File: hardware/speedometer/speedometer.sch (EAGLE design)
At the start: 124 parts, among them IC1 PIC32MX274F256DT-I_PT, IC10 24LC024SN, IC11 MAX16054AZT+T, IC12 TPS63001DRCT, IC13 TPS63002DRCT, IC2 CSTCE8M00G55-R0, IC3 BQ27441DRZR-G1A, IC7 BQ24075RGTT, IC8 NRF24L01P-T, IC9 CSTCE16M0V53-R0, J1 10104111-0001LF, J2 BAT, J3 CONUFL001-SMD-T, J4 Right_sens, J5 Right, J6 Left_sens, J7 Left, Q1 BC817, Q2 BC817, Q3 BC817, Q4 BC817, U1 SN74AHC1G08DBVR

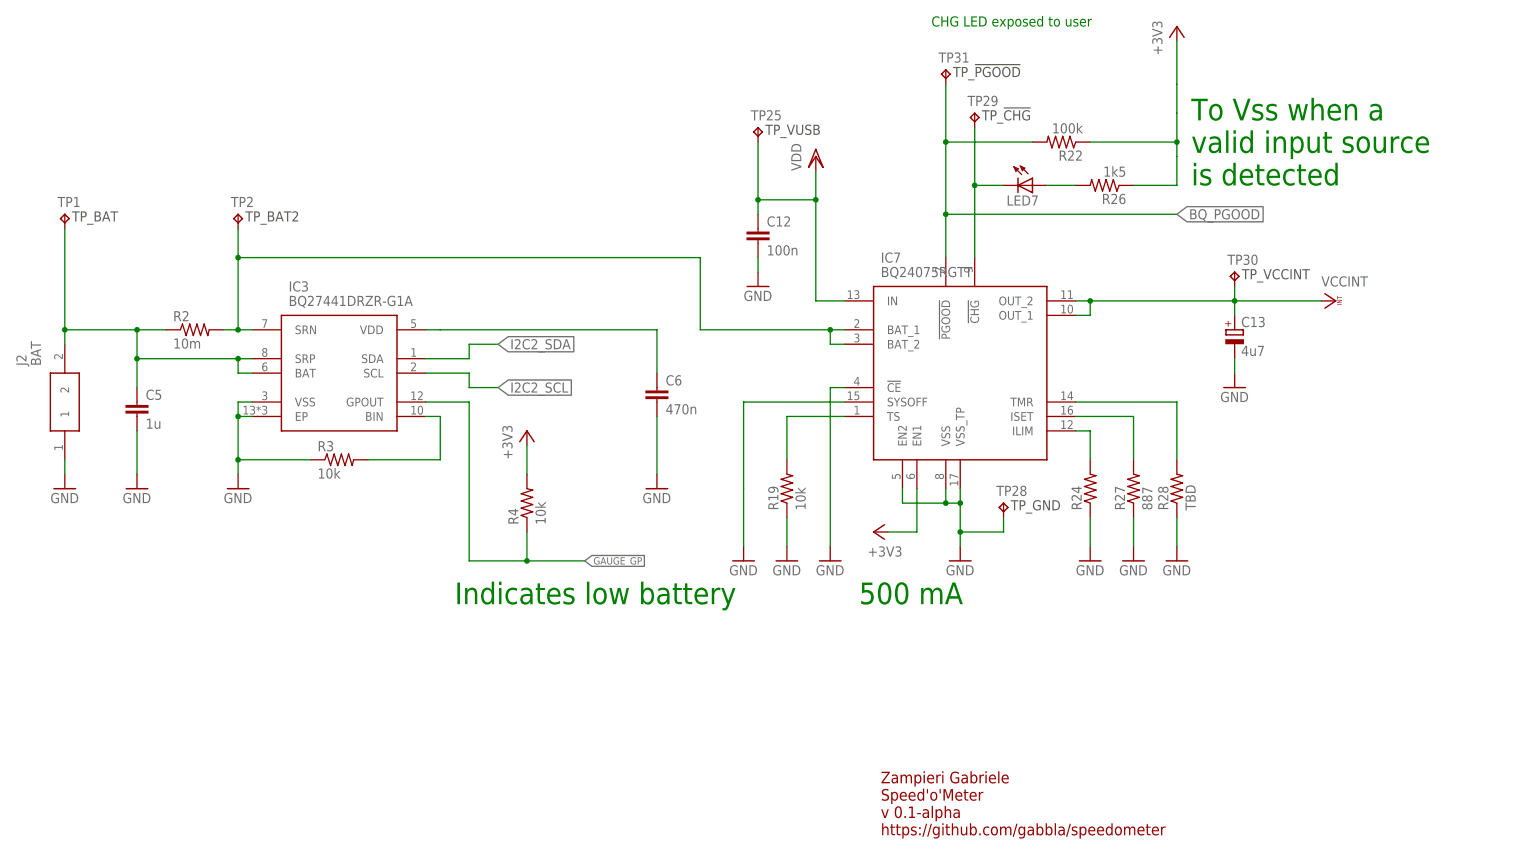
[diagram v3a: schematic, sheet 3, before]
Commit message: fixed led off while charging the board in off state
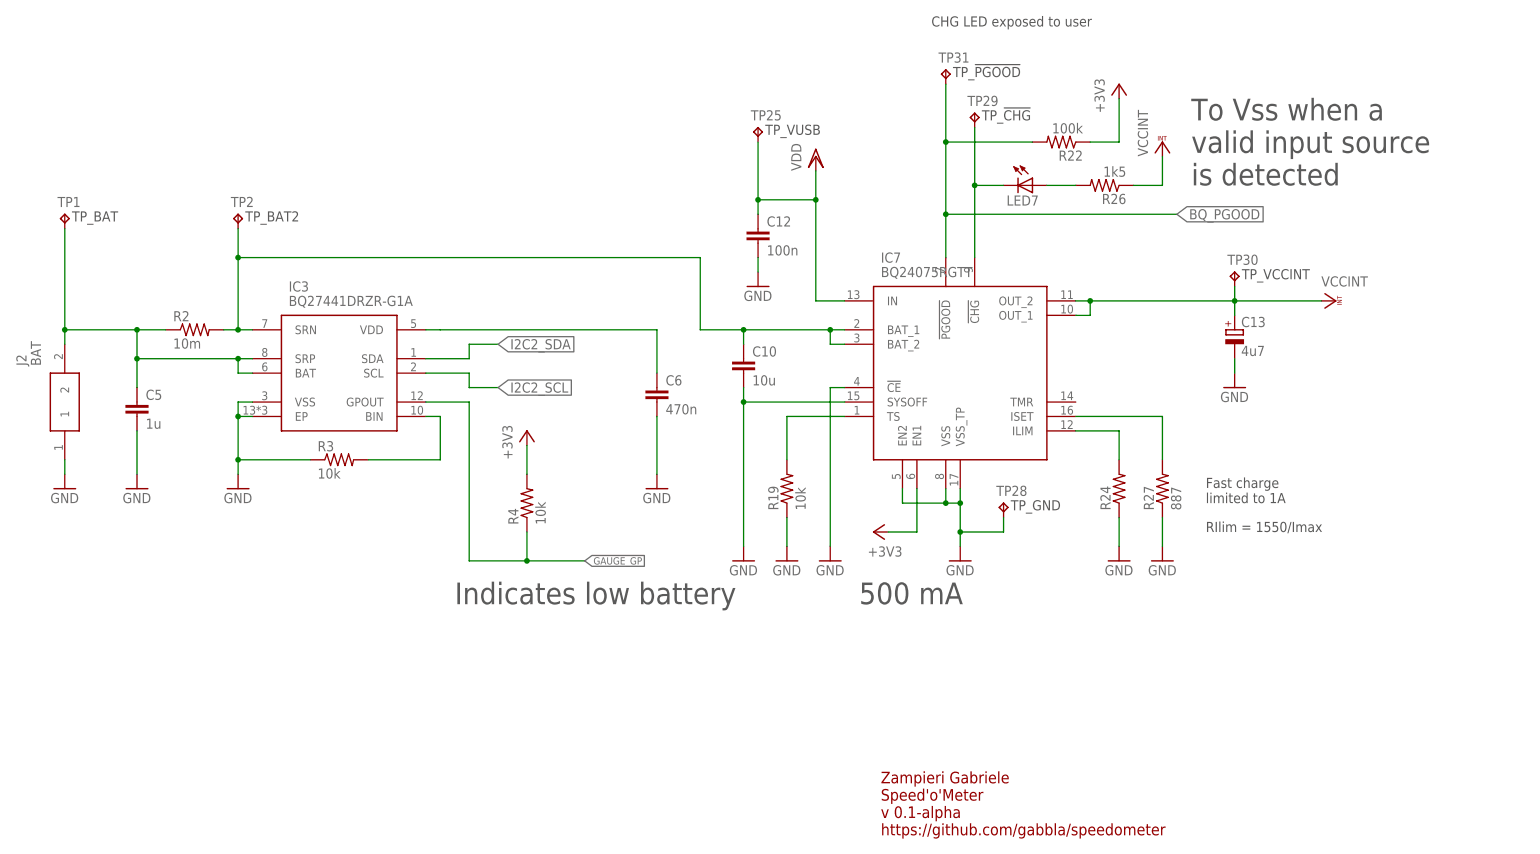
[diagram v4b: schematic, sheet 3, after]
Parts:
- removed R28: TBD, rcl:R-US_R0805
- added C10: 10u, rcl:C-EUC0603K
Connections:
- removed net N$14: IC7.TMR, R28.2
- net +3V3: no longer R26.1
- net GND: now also C10.2; no longer R28.1
- net N$43: now also C10.1
- net VCCINT: now also R26.1
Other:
- note added: "Fast charge limited to 1A"
- note added: "RIlim = 1550/Imax"
- moved on the sheet: R24, R27

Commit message: part renumbered
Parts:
- removed C29, C30: 10u, rcl:C-EUC0805K
- removed IC12: TPS63001DRCT, TPS63000DRCT:TPS63000DRCT
- removed IC13: TPS63002DRCT, TPS63000DRCT:TPS63000DRCT
- removed R35, R39: 100k, rcl:R-US_R0805
- removed R36, R37: 100, rcl:R-US_R0805
- removed R38: 10k, rcl:R-US_R0805
- removed TP25, TP31: TPB1,27, testpad:TPB1,27
- removed U$1: HM-11, HM11:HM-11
- added C11: 100n, rcl:C-EUC0603K
- added C16: 2n2, rcl:C-EUC0402K
- added IC4: BQ27441DRZR-G1A, BQ27441DRZR-G1A:BQ27441DRZR-G1A
- added IC5: BQ24075RGTT, BQ24075RGTT:BQ24075RGTT
- added IC6: NRF24L01P-T, nRF24L01P-T:NRF24L01P-T
- added R15, R33: 100k, rcl:R-US_R0805
- added R16: 1k5, rcl:R-US_R0805
- added R17: (no value), rcl:R-US_R0805
- added R31: 10k, rcl:R-US_R0805
- added TP14, TP9: TPB1,27, testpad:TPB1,27
- C1: value 10u -> 100n; device rcl:C-EUC0805K -> rcl:C-EUC0603
- C12: value 100n -> 4u7; device rcl:C-EUC0603K -> rcl:CPOL-EUSMCA
- C13: value 4u7 -> 10n; device rcl:CPOL-EUSMCA -> rcl:C-EUC0805K
- C14: value 10n -> 1n
- C15: value 1n -> 33n; device rcl:C-EUC0805K -> rcl:C-EUC0402K
- C17: value 33n -> 4p7
- C18: value 2n2 -> 1p5
- C19: value 4p7 -> 1p
- C20: value 1p5 -> 100n; device rcl:C-EUC0402K -> rcl:C-EUC0603K
- C21: value 1p -> 10u; device rcl:C-EUC0402K -> rcl:C-EUC0805K
- C22: value 100n -> 10u; device rcl:C-EUC0603K -> rcl:C-EUC0805K
- C3: value 100n -> 10u; device rcl:C-EUC0603 -> rcl:C-EUC0805K
- C5: value 1u -> 100n; device rcl:C-EUC0603K -> rcl:C-EUC0603
- C6: value 470n -> 100n; device rcl:C-EUC0603K -> rcl:C-EUC0603
- C8: value 100n -> 1u; device rcl:C-EUC0603 -> rcl:C-EUC0603K
- C9: value 100n -> 470n; device rcl:C-EUC0603 -> rcl:C-EUC0603K
- IC10: value 24LC024SN -> TPS63001DRCT; device microchip:24LC024SN -> TPS63000DRCT:TPS63000DRCT
- IC11: value MAX16054AZT+T -> TPS63002DRCT; device MAX16054AZT+T:MAX16054AZT+T -> TPS63000DRCT:TPS63000DRCT
- IC3: value BQ27441DRZR-G1A -> HM-11; device BQ27441DRZR-G1A:BQ27441DRZR-G1A -> HM11:HM-11
- IC7: value BQ24075RGTT -> CSTCE16M0V53-R0; device BQ24075RGTT:BQ24075RGTT -> CSTCE12M0G15L99-R0:CSTCE12M0G15L99-R0
- IC8: value NRF24L01P-T -> 24LC024SN; device nRF24L01P-T:NRF24L01P-T -> microchip:24LC024SN
- IC9: value CSTCE16M0V53-R0 -> MAX16054AZT+T; device CSTCE12M0G15L99-R0:CSTCE12M0G15L99-R0 -> MAX16054AZT+T:MAX16054AZT+T
- JP2: device pinhead:PINHD-1X3 -> pinhead:PINHD-1X2
- JP3: device pinhead:PINHD-1X2 -> pinhead:PINHD-1X3
- LED1: device led:LED3MM -> led:LEDCHIPLED_0805
- LED2: device led:LEDCHIPLED_0805 -> led:LED3MM
- Q2: SPICEPREFIX Q -> (none)
- Q3: SPICEPREFIX (none) -> Q
- R11: value 470 -> 10m; device rcl:R-US_M0805 -> rcl:R-US_R2512; RS (none) -> 693-4381
- R13: value 1k -> 10k; device rcl:R-US_M0805 -> rcl:R-US_R0805
- R14: device rcl:R-US_M0805 -> rcl:R-US_R0805
- R18: value 100k -> 887; RS (none) -> 708-6111
- R19: value 10k -> 22k
- R2: value 10m -> 1k; device rcl:R-US_R2512 -> rcl:R-US_M0805; RS 693-4381 -> (none)
- R20, R25: value 10k -> 100k
- R21: value 10k -> 100; RS_PART_NUMBER (none) -> 740-8978
- R22: value 100k -> 100; RS_PART_NUMBER (none) -> 740-8978
- R23: value 100k -> 10k
- R24: value (none) -> 10k
- R26: value 1k5 -> 10k
- R27: value 887 -> 100k; RS 708-6111 -> (none)
- R3, R4: device rcl:R-US_R0805 -> rcl:R-US_M0805
- R34: value 22k -> 10k
- R7: value 10k -> 4k7
- R9: value 4k7 -> 470
- TP1: TP_SIGNAL_NAME TP_BAT -> TP_SCL
- TP10: TP_SIGNAL_NAME TP_SPI1_SCK -> BT_RX
- TP11: TP_SIGNAL_NAME TP_NRF_CE -> BT_RST
- TP12: TP_SIGNAL_NAME BT_TX -> BT_KEY
- TP13: TP_SIGNAL_NAME BT_RX -> TP_BAT
- TP15: TP_SIGNAL_NAME BT_RST -> TP_VUSB
- TP16: TP_SIGNAL_NAME BT_KEY -> TP_!PGOOD
- TP2: TP_SIGNAL_NAME TP_BAT2 -> TP_SDA
- TP3: TP_SIGNAL_NAME TP_SCL -> TP_SPI1_SDO
- TP4: TP_SIGNAL_NAME TP_SDA -> TP_SPI1_SDI
- TP5: TP_SIGNAL_NAME TP_SPI1_SDO -> TP_NRF_IRQ
- TP6: TP_SIGNAL_NAME TP_SPI1_SDI -> TP_NRF_CS
- TP7: TP_SIGNAL_NAME TP_NRF_IRQ -> TP_SPI1_SCK
- TP8: TP_SIGNAL_NAME TP_NRF_CS -> TP_NRF_CE
- renumbered ICSP to SV1, LED7 to LED3, LED8 to LED4, LED9 to LED5, R40 to R28, R41 to R29, R42 to R30, R43 to R32, TP28 to TP18, TP29 to TP17, TP30 to TP19, TP33 to TP20, TP34 to TP21, TP35 to TP22, TP36 to TP23, TP37 to TP24
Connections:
- net !BAT_CHG: now also IC5.!CHG; no longer IC7.!CHG
- net !MCLR: now also R2.1; no longer R13.1
- net +3V3: now also C1.1, C13.1, C20.1, C5.1, IC10.FB, IC10.VOUT, IC3.VCC, IC5.EN1, IC6.VDD_1, IC6.VDD_2, IC6.VDD_3, IC8.VCC, JP2.1, R13.2, R15.1, R26.2, R3.2, R34.2; no longer C15.1, C22.1, C3.1, C8.1, IC10.VCC, IC12.FB, IC12.VOUT, IC7.EN1, IC8.VDD_1, IC8.VDD_2, IC8.VDD_3, JP3.1, R22.1, R25.2, R35.2, R4.2, R9.2, U$1.VCC
- net +5V: now also IC11.FB, IC11.VOUT; no longer IC13.FB, IC13.VOUT
- net BL_TRIG: now also JP2.2, R4.2; no longer JP3.2, R14.2
- net BQ_PGOOD: now also IC5.!PGOOD, R15.2, TP16.TP; no longer IC7.!PGOOD, R22.2, TP31.TP
- net BT_RST: now also R7.1; no longer R9.1
- net GAUGE_GP: now also IC4.GPOUT, R13.1; no longer IC3.GPOUT, R4.1
- net GND: now also C11.2, C12.-, C13.2, C16.2, C20.2, IC10.PGND, IC11.PGND, IC3.GND, IC4.EP, IC4.VSS, IC5.!CE, IC5.EN2, IC5.SYSOFF, IC5.VSS, IC5.VSS_TP, IC6.TP_GND, IC6.VSS_1, IC6.VSS_2, IC6.VSS_3, IC6.VSS_4, IC7.2, IC8.A0, IC8.A1, IC8.A2, IC8.GND, IC8.WP, IC9.CLEAR, IC9.GND, JP3.3, LED2.C, R12.1, R17.1, R18.1, R19.2, R25.2, R27.2, R33.2, R4.1; no longer C12.2, C13.-, C18.2, C29.2, C30.2, IC10.A0, IC10.A1, IC10.A2, IC10.WP, IC11.CLEAR, IC12.GND, IC12.PGND, IC13.GND, IC13.PGND, IC3.EP, IC3.VSS, IC7.!CE, IC7.EN2, IC7.SYSOFF, IC7.VSS, IC7.VSS_TP, IC8.TP_GND, IC8.VSS_1, IC8.VSS_2, IC8.VSS_3, IC8.VSS_4, IC9.2, JP2.3, LED1.C, R18.2, R19.1, R23.2, R24.1, R27.1, R3.1, R34.2, R39.2, U$1.GND
- net I2C2_SCL: now also IC4.SCL, IC8.SCL, TP1.TP; no longer IC10.SCL, IC3.SCL, TP3.TP
- net I2C2_SDA: now also IC4.SDA, IC8.SDA, TP2.TP; no longer IC10.SDA, IC3.SDA, TP4.TP
- net INT_LEFT: now also R34.1; no longer R25.1
- net INT_RIGHT: now also Q1.C, R26.1; no longer Q3.C, R20.1
- net LED_HB: now also LED1.A; no longer LED2.A
- net N$1: now also IC3.!RESET, TP11.TP; no longer TP15.TP, U$1.!RESET
- net N$12: now also R16.2; no longer R26.2
- net N$13: now also R31.2, R33.1; no longer R21.2, R23.1
- net N$16: now also C9.1, IC4.VDD; no longer C6.1, IC3.VDD
- net N$17: now also Q3.C; no longer Q2.C
- net N$18: now also Q3.B; no longer Q2.B
- net N$2: now also IC3.PIO0/KEY, TP12.TP; no longer TP16.TP, U$1.PIO0/KEY
- net N$21: now also C3.1; no longer C1.1
- net N$22: now also IC6.XC2, IC7.1; no longer IC8.XC2, IC9.1
- net N$24: now also IC6.IREF, R19.1; no longer IC8.IREF, R34.1
- net N$25: now also C15.1, IC6.DVDD; no longer C17.1, IC8.DVDD
- net N$26: now also Q1.B, R23.2, R25.1; no longer Q3.B, R12.2, R18.1
- net N$27: now also R23.1; no longer R12.1
- net N$28: now also R31.1; no longer R21.1
- net N$29: now also LED1.C; no longer LED2.C
- net N$3: now also C8.1, IC4.BAT, IC4.SRP, R11.1, TP13.TP; no longer C5.1, IC3.BAT, IC3.SRP, R2.1, TP1.TP
- net N$30: now also IC4.BIN, R12.2; no longer IC3.BIN, R3.2
- net N$31: now also IC6.XC1, IC7.3; no longer IC8.XC1, IC9.3
- net N$32: now also IC6.ANT2; no longer IC8.ANT2
- net N$33: now also IC6.ANT1; no longer IC8.ANT1
- net N$34: now also IC10.L2; no longer IC12.L2
- net N$35: now also C16.1, C17.1, IC6.VDD_PA; no longer C18.1, C19.1, IC8.VDD_PA
- net N$36: now also C18.1; no longer C20.1
- net N$37: now also C18.2, C19.1; no longer C20.2, C21.1
- net N$38: now also Q2.C; no longer Q1.C
- net N$39: now also Q2.B, R24.2, R27.1; no longer Q1.B, R38.2, R39.1
- net N$4: now also IC3.PIO1/LED, R9.1; no longer R11.1, U$1.PIO1/LED
- net N$41: now also C6.1, R2.2, R3.1; no longer C9.1, R13.2, R7.1
- net N$42: now also R24.1; no longer R38.1
- net N$43: now also IC4.SRN, IC5.BAT_1, IC5.BAT_2, R11.2, TP14.TP; no longer IC3.SRN, IC7.BAT_1, IC7.BAT_2, R2.2, TP2.TP
- net N$5: now also IC10.L1; no longer IC12.L1
- net N$58: now also IC9.IN; no longer IC11.IN
- net N$59: now also IC11.L1; no longer IC13.L1
- net N$6: now also LED2.A, R9.2; no longer LED1.A, R11.2
- net N$60: now also IC10.PS/SYNC, IC10.VINA, R21.1; no longer IC12.PS/SYNC, IC12.VINA, R36.1
- net N$61: now also IC11.L2; no longer IC13.L2
- net N$62: now also IC11.PS/SYNC, IC11.VINA, R22.1; no longer IC13.PS/SYNC, IC13.VINA, R37.1
- net N$7: now also IC5.TS, R14.2; no longer IC7.TS, R19.2
- net N$8: now also IC5.ILIM, R17.2; no longer IC7.ILIM, R24.2
- net N$9: now also IC5.ISET, R18.2; no longer IC7.ISET, R27.2
- net NRF_!CS: now also IC6.CSN, TP6.TP; no longer IC8.CSN, TP8.TP
- net NRF_CE: now also IC6.CE, TP8.TP; no longer IC8.CE, TP11.TP
- net NRF_IRQ: now also IC6.IRQ, R20.1, TP5.TP; no longer IC8.IRQ, R35.1, TP7.TP
- net SPI1_SCK: now also IC6.SCK, TP7.TP; no longer IC8.SCK, TP10.TP
- net SPI1_SDI: now also IC6.MISO, TP4.TP; no longer IC8.MISO, TP6.TP
- net SPI1_SDO: now also IC6.MOSI, TP3.TP; no longer IC8.MOSI, TP5.TP
- net SYS_EN: now also IC10.EN, IC11.EN, IC9.OUT; no longer IC11.OUT, IC12.EN, IC13.EN
- net U1_RX: now also IC3.UART_TX, TP9.TP; no longer TP12.TP, U$1.UART_TX
- net U1_TX: now also IC3.UART_RX, TP10.TP; no longer TP13.TP, U$1.UART_RX
- net U2_RX: now also JP3.2; no longer JP2.2
- net U2_TX: now also JP3.1; no longer JP2.1
- net VCCINT: now also C12.+, C21.1, C22.1, IC10.VIN, IC11.VIN, IC5.OUT_1, IC5.OUT_2, IC9.VCC, R16.1, R21.2, R22.2; no longer C13.+, C29.1, C30.1, IC11.VCC, IC12.VIN, IC13.VIN, IC7.OUT_1, IC7.OUT_2, R26.1, R36.2, R37.2
- net VDD: now also C11.1, IC5.IN, TP15.TP; no longer C12.1, IC7.IN, TP25.TP

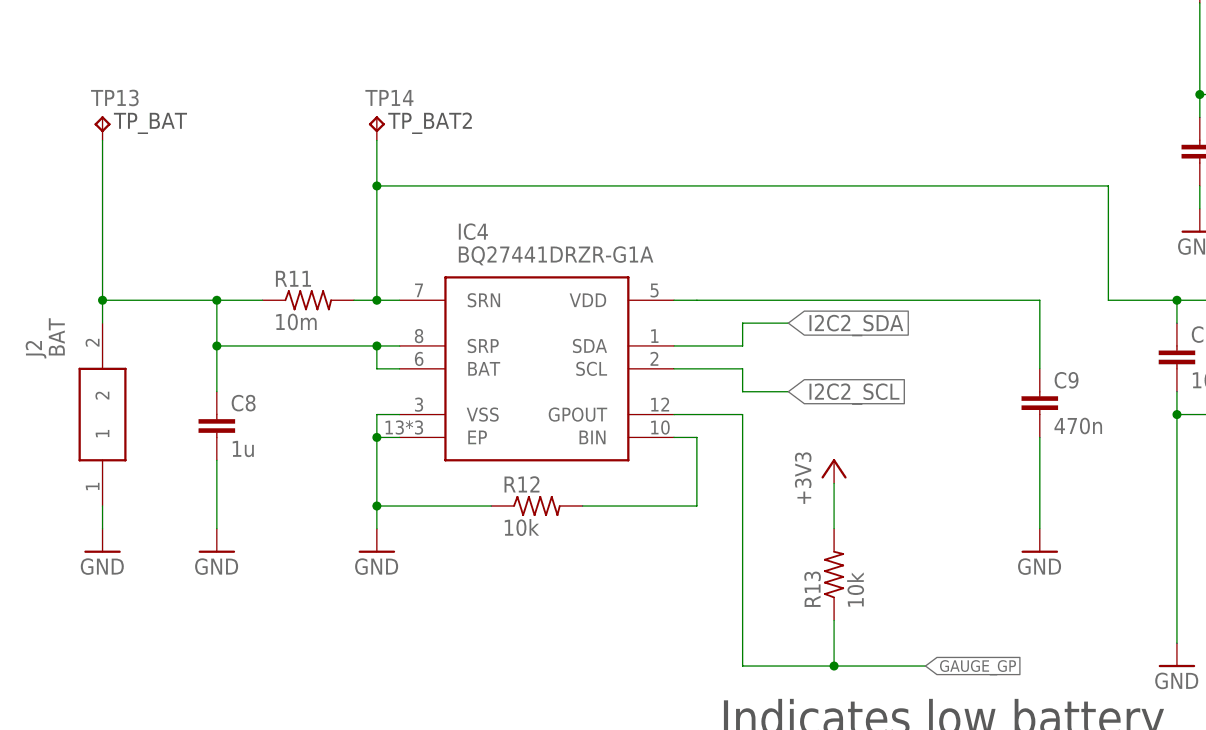
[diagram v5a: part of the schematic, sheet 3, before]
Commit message: pcb: power routed
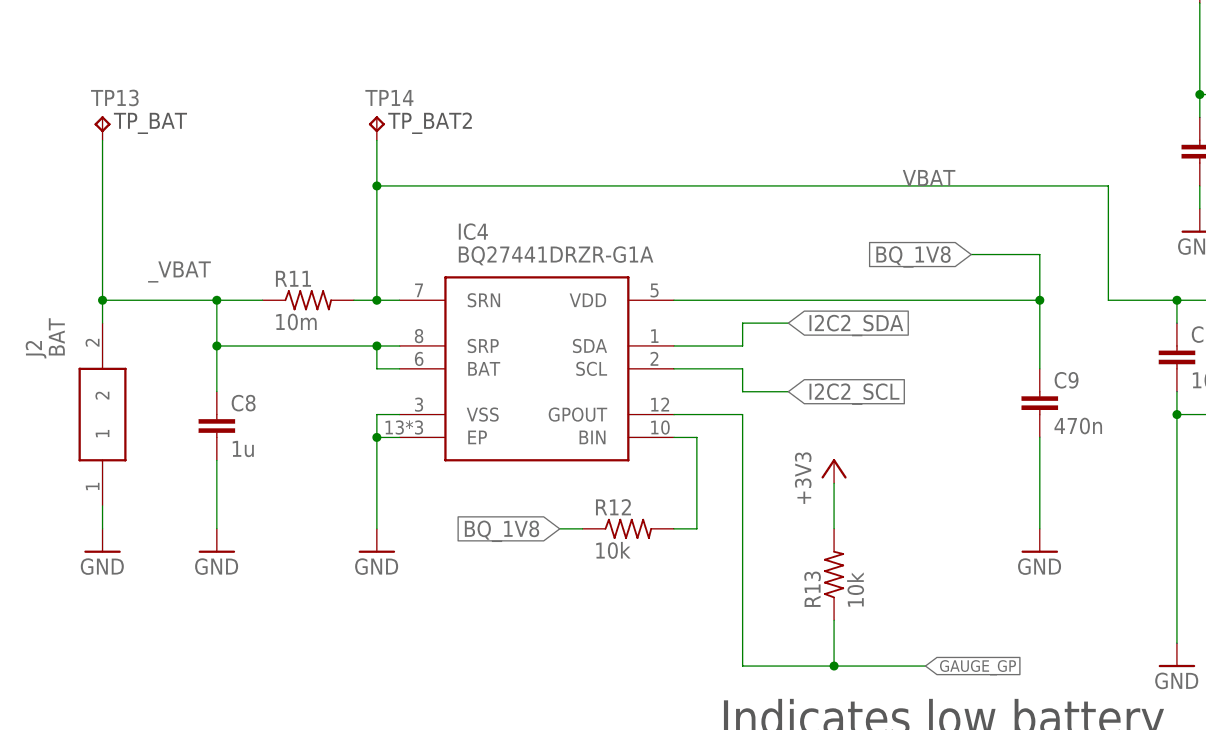
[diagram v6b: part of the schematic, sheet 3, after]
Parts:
- C10, C8, C9: device rcl:C-EUC0603K -> rcl:C-EUC0805K
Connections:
- net N$3 renamed _VBAT
- net N$43 renamed VBAT
- removed net N$16: C9.1, IC4.VDD
- new net BQ_1V8: C9.1, IC4.VDD, R12.1
- net GND: no longer R12.1
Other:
- moved on the sheet: R12
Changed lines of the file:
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@@
 <part name="+3V313" library="supply1" library_urn="urn:adsk.eagle:library:371" deviceset="+3V3" device=""/>
 <part name="IC4" library="BQ27441DRZR-G1A" deviceset="BQ27441DRZR-G1A" device=""/>
-<part name="C8" library="rcl" library_urn="urn:adsk.eagle:library:334" deviceset="C-EU" device="C0603K" package3d_urn="urn:adsk.eagle:package:23680/2" value="1u"/>
+<part name="C8" library="rcl" library_urn="urn:adsk.eagle:library:334" deviceset="C-EU" device="C0805K" package3d_urn="urn:adsk.eagle:package:23681/2" value="1u"/>
 <part name="GND19" library="supply1" library_urn="urn:adsk.eagle:library:371" deviceset="GND" device=""/>
 <part name="GND18" library="supply1" library_urn="urn:adsk.eagle:library:371" deviceset="GND" device=""/>
-<part name="C9" library="rcl" library_urn="urn:adsk.eagle:library:334" deviceset="C-EU" device="C0603K" package3d_urn="urn:adsk.eagle:package:23680/2" value="470n"/>
+<part name="C9" library="rcl" library_urn="urn:adsk.eagle:library:334" deviceset="C-EU" device="C0805K" package3d_urn="urn:adsk.eagle:package:23681/2" value="470n"/>
 <part name="GND20" library="supply1" library_urn="urn:adsk.eagle:library:371" deviceset="GND" device=""/>
 <part name="IC3" library="HM11" deviceset="HM-11" device=""/>
@@
 <part name="+3V322" library="supply1" library_urn="urn:adsk.eagle:library:371" deviceset="+3V3" device=""/>
 <part name="VDD2" library="supply1" library_urn="urn:adsk.eagle:library:371" deviceset="VDD" device=""/>
-<part name="C10" library="rcl" library_urn="urn:adsk.eagle:library:334" deviceset="C-EU" device="C0603K" package3d_urn="urn:adsk.eagle:package:23680/2" value="10u"/>
+<part name="C10" library="rcl" library_urn="urn:adsk.eagle:library:334" deviceset="C-EU" device="C0805K" package3d_urn="urn:adsk.eagle:package:23681/2" value="10u"/>
 <part name="VCC1" library="supply1" library_urn="urn:adsk.eagle:library:371" deviceset="VCCINT" device=""/>
 </parts>
@@
 <attribute name="VALUE" x="39.37" y="93.218" size="1.778" layer="96"/>
 </instance>
-<instance part="R12" gate="G$1" x="68.58" y="73.66" smashed="yes">
-<attribute name="NAME" x="64.77" y="75.1586" size="1.778" layer="95"/>
-<attribute name="VALUE" x="64.77" y="70.358" size="1.778" layer="96"/>
+<instance part="R12" gate="G$1" x="78.74" y="71.12" smashed="yes">
+<attribute name="NAME" x="74.93" y="72.6186" size="1.778" layer="95"/>
+<attribute name="VALUE" x="74.93" y="67.818" size="1.778" layer="96"/>
 </instance>
 <instance part="R13" gate="G$1" x="101.6" y="66.04" smashed="yes" rot="R90">
@@
 <wire x1="50.8" y1="83.82" x2="50.8" y2="81.28" width="0.1524" layer="91"/>
 <pinref part="GND19" gate="1" pin="GND"/>
-<wire x1="50.8" y1="81.28" x2="50.8" y2="73.66" width="0.1524" layer="91"/>
+<wire x1="50.8" y1="81.28" x2="50.8" y2="71.12" width="0.1524" layer="91"/>
 <pinref part="IC4" gate="G$1" pin="EP"/>
-<wire x1="50.8" y1="73.66" x2="50.8" y2="71.12" width="0.1524" layer="91"/>
 <wire x1="53.34" y1="81.28" x2="50.8" y2="81.28" width="0.1524" layer="91"/>
 <junction x="50.8" y="81.28"/>
-<pinref part="R12" gate="G$1" pin="1"/>
-<wire x1="63.5" y1="73.66" x2="50.8" y2="73.66" width="0.1524" layer="91"/>
-<junction x="50.8" y="73.66"/>
 </segment>
 <segment>
@@
 </segment>
 </net>
-<net name="N$3" class="0">
+<net name="_VBAT" class="0">
 <segment>
 <pinref part="R11" gate="G$1" pin="1"/>
@@
 <wire x1="20.32" y1="114.3" x2="20.32" y2="96.52" width="0.1524" layer="91"/>
 <junction x="20.32" y="96.52"/>
+<label x="25.4" y="99.06" size="1.778" layer="95"/>
 </segment>
 </net>
@@
 </segment>
 </net>
-<net name="N$16" class="0">
+<net name="BQ_1V8" class="0">
 <segment>
 <pinref part="IC4" gate="G$1" pin="VDD"/>
-<wire x1="83.82" y1="96.52" x2="86.36" y2="96.52" width="0.1524" layer="91"/>
-<wire x1="86.36" y1="96.52" x2="124.46" y2="96.52" width="0.1524" layer="91"/>
+<wire x1="83.82" y1="96.52" x2="124.46" y2="96.52" width="0.1524" layer="91"/>
 <pinref part="C9" gate="G$1" pin="1"/>
 <wire x1="124.46" y1="96.52" x2="124.46" y2="88.9" width="0.1524" layer="91"/>
-</segment>
-</net>
-<net name="N$43" class="0">
+<wire x1="124.46" y1="96.52" x2="124.46" y2="101.6" width="0.1524" layer="91"/>
+<junction x="124.46" y="96.52"/>
+<wire x1="124.46" y1="101.6" x2="116.84" y2="101.6" width="0.1524" layer="91"/>
+<label x="116.84" y="101.6" size="1.778" layer="95" font="vector" rot="R180" xref="yes"/>
+</segment>
+<segment>
+<pinref part="R12" gate="G$1" pin="1"/>
+<wire x1="73.66" y1="71.12" x2="71.12" y2="71.12" width="0.1524" layer="91"/>
+<label x="71.12" y="71.12" size="1.778" layer="95" font="vector" rot="R180" xref="yes"/>
+</segment>
+</net>
+<net name="VBAT" class="0">
 <segment>
 <pinref part="R11" gate="G$1" pin="2"/>
@@
 <wire x1="139.7" y1="93.98" x2="139.7" y2="96.52" width="0.1524" layer="91"/>
 <junction x="139.7" y="96.52"/>
+<label x="109.22" y="109.22" size="1.778" layer="95"/>
 </segment>
 </net>
@@
 <segment>
 <pinref part="R12" gate="G$1" pin="2"/>
-<wire x1="73.66" y1="73.66" x2="86.36" y2="73.66" width="0.1524" layer="91"/>
-<wire x1="86.36" y1="73.66" x2="86.36" y2="81.28" width="0.1524" layer="91"/>
+<wire x1="83.82" y1="71.12" x2="86.36" y2="71.12" width="0.1524" layer="91"/>
+<wire x1="86.36" y1="71.12" x2="86.36" y2="81.28" width="0.1524" layer="91"/>
 <pinref part="IC4" gate="G$1" pin="BIN"/>
 <wire x1="86.36" y1="81.28" x2="83.82" y2="81.28" width="0.1524" layer="91"/>
